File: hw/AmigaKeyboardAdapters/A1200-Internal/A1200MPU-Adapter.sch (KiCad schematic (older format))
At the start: 8 parts, among them P1 CONN_02X03, U1 A1200U13_REV_PLCC44

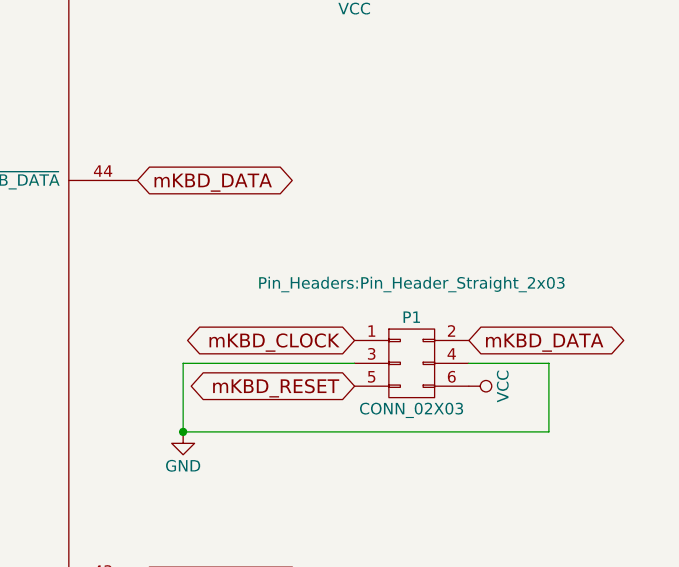
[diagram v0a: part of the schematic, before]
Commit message: Added the idc 2x3 box
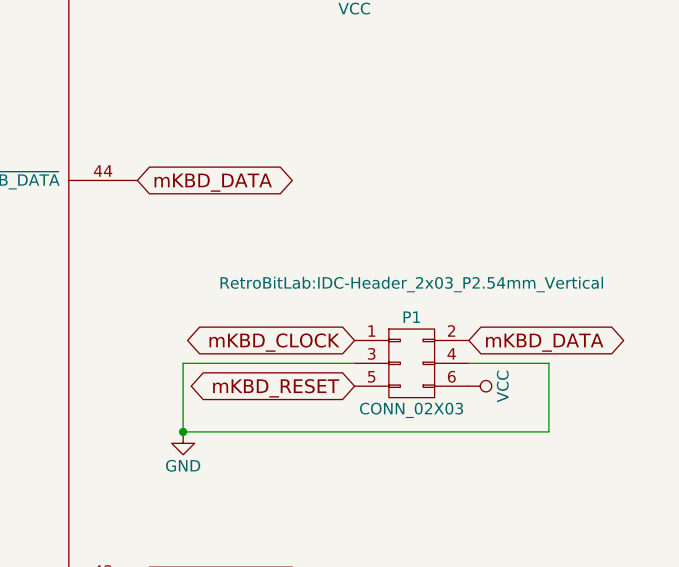
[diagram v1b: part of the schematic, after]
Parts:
- P1: footprint Pin_Headers:Pin_Header_Straight_2x03 -> RetroBitLab:IDC-Header_2x03_P2.54mm_Vertical
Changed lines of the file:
@@
 LIBS:valves
 LIBS:AmigaComponents
+LIBS:4xxx
+LIBS:4xxx_IEEE
+LIBS:74xGxx
+LIBS:74xx_IEEE
+LIBS:Amplifier_Audio
+LIBS:Amplifier_Buffer
+LIBS:Amplifier_Current
+LIBS:Amplifier_Difference
+LIBS:Amplifier_Instrumentation
+LIBS:Amplifier_Operational
+LIBS:Amplifier_Video
+LIBS:Analog
+LIBS:Analog_ADC
+LIBS:Analog_DAC
+LIBS:Analog_Switch
+LIBS:Audio
+LIBS:Battery_Management
+LIBS:Comparator
+LIBS:Connector
+LIBS:Connector_Generic
+LIBS:Connector_Generic_MountingPin
+LIBS:Connector_Generic_Shielded
+LIBS:Converter_ACDC
+LIBS:Converter_DCDC
+LIBS:CPLD_Altera
+LIBS:CPLD_Xilinx
+LIBS:CPU
+LIBS:CPU_NXP_6800
+LIBS:CPU_NXP_68000
+LIBS:CPU_PowerPC
+LIBS:Device
+LIBS:Diode
+LIBS:Diode_Bridge
+LIBS:Diode_Laser
+LIBS:Display_Character
+LIBS:Display_Graphic
+LIBS:Driver_Display
+LIBS:Driver_FET
+LIBS:Driver_LED
+LIBS:Driver_Motor
+LIBS:Driver_Relay
+LIBS:DSP_AnalogDevices
+LIBS:DSP_Freescale
+LIBS:DSP_Microchip_DSPIC33
+LIBS:DSP_Motorola
+LIBS:DSP_Texas
+LIBS:Fiber_Optic
+LIBS:Filter
+LIBS:FPGA_Lattice
+LIBS:FPGA_Microsemi
+LIBS:FPGA_Xilinx
+LIBS:FPGA_Xilinx_Artix7
+LIBS:FPGA_Xilinx_Kintex7
+LIBS:FPGA_Xilinx_Spartan6
+LIBS:FPGA_Xilinx_Virtex5
+LIBS:FPGA_Xilinx_Virtex6
+LIBS:FPGA_Xilinx_Virtex7
+LIBS:ft232rl
+LIBS:GPU
+LIBS:Graphic
+LIBS:Interface
+LIBS:Interface_CAN_LIN
+LIBS:Interface_CurrentLoop
+LIBS:Interface_Ethernet
+LIBS:Interface_Expansion
+LIBS:Interface_HID
+LIBS:Interface_LineDriver
+LIBS:Interface_Optical
+LIBS:Interface_Telecom
+LIBS:Interface_UART
+LIBS:Interface_USB
+LIBS:Isolator
+LIBS:Isolator_Analog
+LIBS:Jumper
+LIBS:LED
+LIBS:Logic_LevelTranslator
+LIBS:Logic_Programmable
+LIBS:MCU_AnalogDevices
+LIBS:MCU_Cypress
+LIBS:MCU_Espressif
+LIBS:MCU_Intel
+LIBS:MCU_Microchip_8051
+LIBS:MCU_Microchip_ATmega
+LIBS:MCU_Microchip_ATtiny
+LIBS:MCU_Microchip_AVR
+LIBS:MCU_Microchip_PIC10
+LIBS:MCU_Microchip_PIC12
+LIBS:MCU_Microchip_PIC16
+LIBS:MCU_Microchip_PIC18
+LIBS:MCU_Microchip_PIC24
+LIBS:MCU_Microchip_PIC32
+LIBS:MCU_Microchip_SAMD
+LIBS:MCU_Microchip_SAME
+LIBS:MCU_Microchip_SAML
+LIBS:MCU_Module
+LIBS:MCU_Nordic
+LIBS:MCU_NXP_ColdFire
+LIBS:MCU_NXP_HC11
+LIBS:MCU_NXP_HC12
+LIBS:MCU_NXP_HCS12
+LIBS:MCU_NXP_Kinetis
+LIBS:MCU_NXP_LPC
+LIBS:MCU_NXP_MAC7100
+LIBS:MCU_NXP_MCore
+LIBS:MCU_NXP_S08
+LIBS:MCU_Parallax
+LIBS:MCU_SiFive
+LIBS:MCU_SiliconLabs
+LIBS:MCU_ST_STM8
+LIBS:MCU_ST_STM32F0
+LIBS:MCU_ST_STM32F1
+LIBS:MCU_ST_STM32F2
+LIBS:MCU_ST_STM32F3
+LIBS:MCU_ST_STM32F4
+LIBS:MCU_ST_STM32F7
+LIBS:MCU_ST_STM32H7
+LIBS:MCU_ST_STM32L0
+LIBS:MCU_ST_STM32L1
+LIBS:MCU_ST_STM32L4
+LIBS:MCU_ST_STM32L4+
+LIBS:MCU_Texas
+LIBS:MCU_Texas_MSP430
+LIBS:Mechanical
+LIBS:Memory_Controller
+LIBS:Memory_EEPROM
+LIBS:Memory_EPROM
+LIBS:Memory_Flash
+LIBS:Memory_NVRAM
+LIBS:Memory_RAM
+LIBS:Memory_ROM
+LIBS:Memory_UniqueID
+LIBS:Motor
+LIBS:Oscillator
+LIBS:Potentiometer_Digital
+LIBS:Power_Management
+LIBS:Power_Protection
+LIBS:Power_Supervisor
+LIBS:pspice
+LIBS:Reference_Current
+LIBS:Reference_Voltage
+LIBS:Regulator_Controller
+LIBS:Regulator_Current
+LIBS:Regulator_Linear
+LIBS:Regulator_SwitchedCapacitor
+LIBS:Regulator_Switching
+LIBS:Relay
+LIBS:Relay_SolidState
+LIBS:RF
+LIBS:RF_AM_FM
+LIBS:RF_Amplifier
+LIBS:RF_Bluetooth
+LIBS:RF_GPS
+LIBS:RF_GSM
+LIBS:RF_Mixer
+LIBS:RF_Module
+LIBS:RF_RFID
+LIBS:RF_Switch
+LIBS:RF_WiFi
+LIBS:RF_ZigBee
+LIBS:Security
+LIBS:Sensor
+LIBS:Sensor_Audio
+LIBS:Sensor_Current
+LIBS:Sensor_Gas
+LIBS:Sensor_Humidity
+LIBS:Sensor_Magnetic
+LIBS:Sensor_Motion
+LIBS:Sensor_Optical
+LIBS:Sensor_Pressure
+LIBS:Sensor_Proximity
+LIBS:Sensor_Temperature
+LIBS:Sensor_Touch
+LIBS:Sensor_Voltage
+LIBS:Switch
+LIBS:Timer
+LIBS:Timer_PLL
+LIBS:Timer_RTC
+LIBS:Transformer
+LIBS:Transistor_Array
+LIBS:Transistor_BJT
+LIBS:Transistor_FET
+LIBS:Transistor_IGBT
+LIBS:Triac_Thyristor
+LIBS:Valve
+LIBS:Video
 LIBS:A1200MPU-Adapter-cache
 EELAYER 25 0
@@
 F 0 "P1" H 7950 3750 50  0000 C CNN
 F 1 "CONN_02X03" H 7950 3350 50  0000 C CNN
-F 2 "Pin_Headers:Pin_Header_Straight_2x03" H 7950 3900 50  0000 C CNN
+F 2 "RetroBitLab:IDC-Header_2x03_P2.54mm_Vertical" H 7950 3900 50  0000 C CNN
 F 3 "" H 7950 2350 50  0000 C CNN
 	1    7950 3550

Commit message: From Kicad 4 to Kicad 5
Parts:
- removed C2: 10uF, SMD_Packages:SMD-1206_Pol, symbol CP1_Small
- removed C4: 100nF, Capacitors_SMD:C_1206_HandSoldering, symbol C_Small
- removed D1: Led_Small, SMD_Packages:SMD-1206_Pol, symbol Led_Small
- removed P1: CONN_02X03, RetroBitLab:IDC-Header_2x03_P2.54mm_Vertical, symbol CONN_02X03
- added C2: 10uF, Capacitor_Tantalum_SMD:CP_EIA-3216-12_Kemet-S_Pad1.58x1.35mm_HandSolder, symbol Device:CP1_Small
- added C4: 100nF, Capacitor_SMD:C_1206_3216Metric_Pad1.33x1.80mm_HandSolder, symbol Device:C_Small
- added D1: RED, LED_SMD:LED_1206_3216Metric_Pad1.42x1.75mm_HandSolder, symbol Device:LED
- added P1: Conn_02x03_Odd_Even, Connector_IDC:IDC-Header_2x03_P2.54mm_Vertical, symbol Connector_Generic:Conn_02x03_Odd_Even
- C1: footprint SMD_Packages:SMD-1206_Pol -> Capacitor_Tantalum_SMD:CP_EIA-3216-12_Kemet-S_Pad1.58x1.35mm_HandSolder; symbol CP1_Small -> Device:CP1_Small; LCSC (none) -> C108529
- C3: footprint Capacitors_SMD:C_1206_HandSoldering -> Capacitor_SMD:C_1206_3216Metric_Pad1.33x1.80mm_HandSolder; symbol C_Small -> Device:C_Small; LCSC (none) -> C24497
- R1: value 330 -> 330R; footprint Resistors_SMD:R_1206_HandSoldering -> Resistor_SMD:R_1206_3216Metric_Pad1.30x1.75mm_HandSolder; symbol R_Small -> Device:R_Small; LCSC (none) -> C245520
- U1: footprint Sockets:PLCC44 -> RetroBitLab:PLCC-44_THT-Socket_3D; symbol A1200U13_REV_PLCC44 -> AmigaComponents:A1200U13_REV_PLCC44
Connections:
- wire segments 17 -> 26
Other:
- moved on the sheet: R1
